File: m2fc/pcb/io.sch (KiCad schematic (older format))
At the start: 28 parts

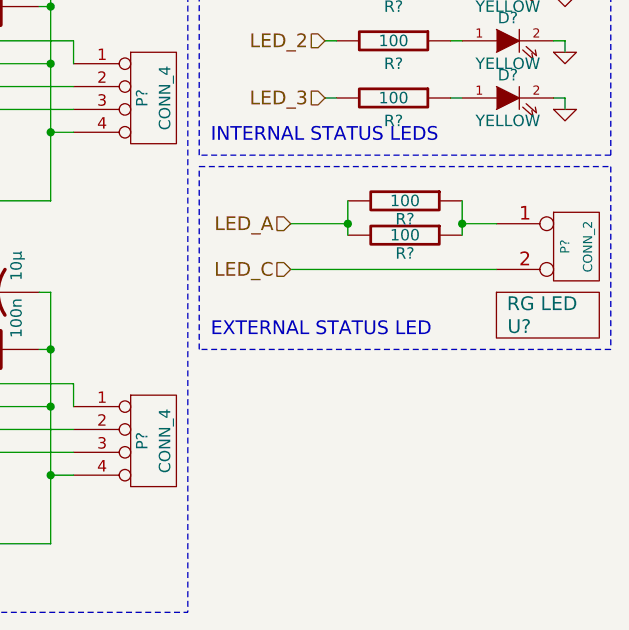
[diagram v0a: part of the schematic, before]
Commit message: rename m2d to m2fc which now incorporates m2p
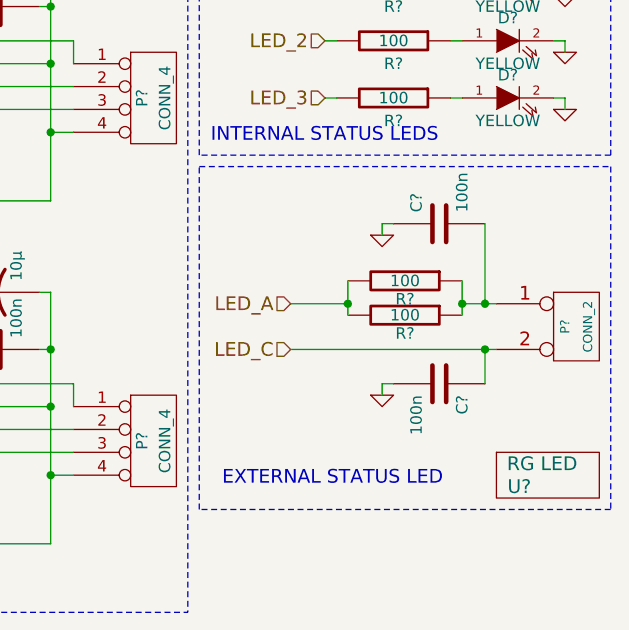
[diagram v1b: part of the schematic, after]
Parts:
- added C? (x2): 100n, 0603, symbol C
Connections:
- net GND: now also C?.1, C?.2
- net LED_C: now also C?.1
- net at P?.1 (P1), R?.1, R?.1: now also C?.2
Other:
- moved on the sheet: P?, R?, U?
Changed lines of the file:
@@
 LIBS:adxl375
 LIBS:apu1205-hf-3
-LIBS:m2d-cache
+LIBS:m2fc-cache
 LIBS:part
 LIBS:sp100-2t
@@
 LIBS:op1177
 LIBS:stm32f415rg
-LIBS:m2d-cache
+LIBS:op2177
+LIBS:microsd
+LIBS:m2fc-cache
 EELAYER 24 0
 EELAYER END
 $Descr A4 11693 8268
 encoding utf-8
-Sheet 5 5
-Title "Martlet 2 Datalogger Board"
-Date "02 Jul 2014"
+Sheet 5 6
+Title "Martlet 2 Flight Computer"
+Date "05 Jul 2014"
 Rev "1"
 Comp "Cambridge University Spaceflight"
@@
 $EndComp
 $Comp
-L GND #PWR?
+L GND #PWR078
 U 1 1 53B6A65A
 P 4200 3400
-F 0 "#PWR?" H 4200 3400 30  0001 C CNN
+F 0 "#PWR078" H 4200 3400 30  0001 C CNN
 F 1 "GND" H 4200 3330 30  0001 C CNN
 F 2 "" H 4200 3400 60  0001 C CNN
@@
 $EndComp
 $Comp
-L GND #PWR?
+L GND #PWR079
 U 1 1 53B6A660
 P 4250 3750
-F 0 "#PWR?" H 4250 3750 30  0001 C CNN
+F 0 "#PWR079" H 4250 3750 30  0001 C CNN
 F 1 "GND" H 4250 3680 30  0001 C CNN
 F 2 "" H 4250 3750 60  0001 C CNN
@@
 $EndComp
 $Comp
-L GND #PWR?
+L GND #PWR080
 U 1 1 53B6A668
 P 3750 3000
-F 0 "#PWR?" H 3750 3000 30  0001 C CNN
+F 0 "#PWR080" H 3750 3000 30  0001 C CNN
 F 1 "GND" H 3750 2930 30  0001 C CNN
 F 2 "" H 3750 3000 60  0001 C CNN
@@
 $EndComp
 $Comp
-L GND #PWR?
+L GND #PWR081
 U 1 1 53B6A69E
 P 4200 4900
-F 0 "#PWR?" H 4200 4900 30  0001 C CNN
+F 0 "#PWR081" H 4200 4900 30  0001 C CNN
 F 1 "GND" H 4200 4830 30  0001 C CNN
 F 2 "" H 4200 4900 60  0001 C CNN
@@
 $EndComp
 $Comp
-L GND #PWR?
+L GND #PWR082
 U 1 1 53B6A6A4
 P 4250 5250
-F 0 "#PWR?" H 4250 5250 30  0001 C CNN
+F 0 "#PWR082" H 4250 5250 30  0001 C CNN
 F 1 "GND" H 4250 5180 30  0001 C CNN
 F 2 "" H 4250 5250 60  0001 C CNN
@@
 $EndComp
 $Comp
-L GND #PWR?
+L GND #PWR083
 U 1 1 53B6A6AC
 P 3750 4500
-F 0 "#PWR?" H 3750 4500 30  0001 C CNN
+F 0 "#PWR083" H 3750 4500 30  0001 C CNN
 F 1 "GND" H 3750 4430 30  0001 C CNN
 F 2 "" H 3750 4500 60  0001 C CNN
@@
 SERIAL IN/OUT
 $Comp
-L +3.3V #PWR?
+L +3.3V #PWR084
 U 1 1 53B6A6B3
 P 4100 5000
-F 0 "#PWR?" H 4100 4960 30  0001 C CNN
+F 0 "#PWR084" H 4100 4960 30  0001 C CNN
 F 1 "+3.3V" H 4100 5110 30  0000 C CNN
 F 2 "" H 4100 5000 60  0000 C CNN
@@
 $EndComp
 $Comp
-L +3.3V #PWR?
+L +3.3V #PWR085
 U 1 1 53B6A6B9
 P 4100 3500
-F 0 "#PWR?" H 4100 3460 30  0001 C CNN
+F 0 "#PWR085" H 4100 3460 30  0001 C CNN
 F 1 "+3.3V" H 4100 3610 30  0000 C CNN
 F 2 "" H 4100 3500 60  0000 C CNN
@@
 Wire Notes Line
 	3300 5500 6300 5500
-Text Notes 6400 4300 0    60   ~ 0
+Text Notes 6450 4950 0    60   ~ 0
 EXTERNAL STATUS LED
 $Comp
 L PART U?
 U 1 1 53B6AD6D
-P 7700 4250
-F 0 "U?" H 7750 4250 60  0000 C CNN
-F 1 "RG LED" H 7850 4350 60  0000 C CNN
-F 2 "" H 7700 4250 60  0001 C CNN
-F 3 "" H 7700 4250 60  0001 C CNN
-F 4 "1142488" H 7700 4250 60  0001 C CNN "Farnell"
-	1    7700 4250
+P 7700 4950
+F 0 "U?" H 7750 4950 60  0000 C CNN
+F 1 "RG LED" H 7850 5050 60  0000 C CNN
+F 2 "" H 7700 4950 60  0001 C CNN
+F 3 "" H 7700 4950 60  0001 C CNN
+F 4 "1142488" H 7700 4950 60  0001 C CNN "Farnell"
+	1    7700 4950
 	1    0    0    -1
 $EndComp
@@
 L CONN_2 P?
 U 1 1 53B6AD75
-P 8000 3900
-F 0 "P?" V 7950 3900 40  0000 C CNN
-F 1 "CONN_2" V 8050 3900 40  0000 C CNN
-F 2 "" H 8000 3900 60  0000 C CNN
-F 3 "" H 8000 3900 60  0000 C CNN
-F 4 "1462926" H 8000 3900 60  0001 C CNN "Farnell"
-	1    8000 3900
+P 8000 4250
+F 0 "P?" V 7950 4250 40  0000 C CNN
+F 1 "CONN_2" V 8050 4250 40  0000 C CNN
+F 2 "" H 8000 4250 60  0000 C CNN
+F 3 "" H 8000 4250 60  0000 C CNN
+F 4 "1462926" H 8000 4250 60  0001 C CNN "Farnell"
+	1    8000 4250
 	1    0    0    -1
 $EndComp
@@
 L R R?
 U 1 1 53B6AD98
-P 7250 3850
-F 0 "R?" V 7330 3850 50  0000 C CNN
-F 1 "100" V 7250 3850 50  0000 C CNN
-F 2 "0603" H 7250 3850 60  0001 C CNN
-F 3 "" H 7250 3850 60  0001 C CNN
-F 4 "2331989" V 7250 3850 60  0001 C CNN "Farnell"
-	1    7250 3850
+P 7250 4200
+F 0 "R?" V 7330 4200 50  0000 C CNN
+F 1 "100" V 7250 4200 50  0000 C CNN
+F 2 "0603" H 7250 4200 60  0001 C CNN
+F 3 "" H 7250 4200 60  0001 C CNN
+F 4 "2331989" V 7250 4200 60  0001 C CNN "Farnell"
+	1    7250 4200
 	0    1    1    0
 $EndComp
@@
 L R R?
 U 1 1 53B6ADA0
-P 7250 3700
-F 0 "R?" V 7330 3700 50  0000 C CNN
-F 1 "100" V 7250 3700 50  0000 C CNN
-F 2 "0603" H 7250 3700 60  0001 C CNN
-F 3 "" H 7250 3700 60  0001 C CNN
-F 4 "2331989" V 7250 3700 60  0001 C CNN "Farnell"
-	1    7250 3700
+P 7250 4050
+F 0 "R?" V 7330 4050 50  0000 C CNN
+F 1 "100" V 7250 4050 50  0000 C CNN
+F 2 "0603" H 7250 4050 60  0001 C CNN
+F 3 "" H 7250 4050 60  0001 C CNN
+F 4 "2331989" V 7250 4050 60  0001 C CNN "Farnell"
+	1    7250 4050
 	0    1    1    0
 $EndComp
 Wire Wire Line
-	6750 4000 7650 4000
-Wire Wire Line
-	7000 3800 6750 3800
-Wire Wire Line
-	7650 3800 7500 3800
+	6750 4350 7650 4350
+Wire Wire Line
+	7000 4150 6750 4150
+Wire Wire Line
+	7500 4150 7650 4150
 Wire Notes Line
 	6350 3550 8150 3550
 Wire Notes Line
-	8150 3550 8150 4350
-Wire Notes Line
-	8150 4350 6350 4350
-Wire Notes Line
-	6350 4350 6350 3550
-Wire Wire Line
-	7000 3700 7000 3850
-Connection ~ 7000 3800
-Wire Wire Line
-	7500 3700 7500 3850
-Connection ~ 7500 3800
+	8150 3550 8150 5050
+Wire Notes Line
+	8150 5050 6350 5050
+Wire Notes Line
+	6350 5050 6350 3550
+Wire Wire Line
+	7000 4050 7000 4200
+Connection ~ 7000 4150
+Wire Wire Line
+	7500 4050 7500 4200
+Connection ~ 7500 4150
 $Comp
 L LED D?
@@
 $EndComp
 $Comp
-L GND #PWR?
+L GND #PWR086
 U 1 1 53B6B193
 P 7600 2550
-F 0 "#PWR?" H 7600 2550 30  0001 C CNN
+F 0 "#PWR086" H 7600 2550 30  0001 C CNN
 F 1 "GND" H 7600 2480 30  0001 C CNN
 F 2 "" H 7600 2550 60  0001 C CNN
@@
 $EndComp
 $Comp
-L GND #PWR?
+L GND #PWR087
 U 1 1 53B6B1AA
 P 7950 2800
-F 0 "#PWR?" H 7950 2800 30  0001 C CNN
+F 0 "#PWR087" H 7950 2800 30  0001 C CNN
 F 1 "GND" H 7950 2730 30  0001 C CNN
 F 2 "" H 7950 2800 60  0001 C CNN
@@
 $EndComp
 $Comp
-L GND #PWR?
+L GND #PWR088
 U 1 1 53B6B1C1
 P 7950 3050
-F 0 "#PWR?" H 7950 3050 30  0001 C CNN
+F 0 "#PWR088" H 7950 3050 30  0001 C CNN
 F 1 "GND" H 7950 2980 30  0001 C CNN
 F 2 "" H 7950 3050 60  0001 C CNN
@@
 $EndComp
 $Comp
-L GND #PWR?
+L GND #PWR089
 U 1 1 53B6B1D8
 P 7950 3300
-F 0 "#PWR?" H 7950 3300 30  0001 C CNN
+F 0 "#PWR089" H 7950 3300 30  0001 C CNN
 F 1 "GND" H 7950 3230 30  0001 C CNN
 F 2 "" H 7950 3300 60  0001 C CNN
@@
 INTERNAL STATUS LEDS
 $Comp
-L +3.3V #PWR?
+L +3.3V #PWR090
 U 1 1 53B6B1DF
 P 6550 2450
-F 0 "#PWR?" H 6550 2410 30  0001 C CNN
+F 0 "#PWR090" H 6550 2410 30  0001 C CNN
 F 1 "+3.3V" H 6550 2560 30  0000 C CNN
 F 2 "" H 6550 2450 60  0000 C CNN
@@
 Text HLabel 3950 4800 0    60   Output ~ 0
 SER_IN_2
-Text HLabel 6750 3800 0    60   Input ~ 0
+Text HLabel 6750 4150 0    60   Input ~ 0
 LED_A
-Text HLabel 6750 4000 0    60   Input ~ 0
+Text HLabel 6750 4350 0    60   Input ~ 0
 LED_C
 Text HLabel 6900 2750 0    60   Input ~ 0
@@
 Connection ~ 4000 3200
 Connection ~ 4000 3300
+$Comp
+L C C?
+U 1 1 53BB2BD1
+P 7400 4500
+F 0 "C?" H 7450 4600 50  0000 L CNN
+F 1 "100n" H 7450 4400 50  0000 L CNN
+F 2 "0603" H 7400 4500 60  0001 C CNN
+F 3 "" H 7400 4500 60  0001 C CNN
+F 4 "1759037" H 7400 4500 60  0001 C CNN "Farnell"
+	1    7400 4500
+	0    1    1    0
+$EndComp
+$Comp
+L C C?
+U 1 1 53BB30F0
+P 7400 3800
+F 0 "C?" H 7450 3900 50  0000 L CNN
+F 1 "100n" H 7450 3700 50  0000 L CNN
+F 2 "0603" H 7400 3800 60  0001 C CNN
+F 3 "" H 7400 3800 60  0001 C CNN
+F 4 "1759037" H 7400 3800 60  0001 C CNN "Farnell"
+	1    7400 3800
+	0    -1   -1   0
+$EndComp
+Wire Wire Line
+	7600 4350 7600 4500
+Connection ~ 7600 4350
+$Comp
+L GND #PWR?
+U 1 1 53BB3222
+P 7150 4550
+F 0 "#PWR?" H 7150 4550 30  0001 C CNN
+F 1 "GND" H 7150 4480 30  0001 C CNN
+F 2 "" H 7150 4550 60  0001 C CNN
+F 3 "" H 7150 4550 60  0001 C CNN
+	1    7150 4550
+	1    0    0    -1
+$EndComp
+Wire Wire Line
+	7200 4500 7150 4500
+Wire Wire Line
+	7150 4500 7150 4550
+$Comp
+L GND #PWR?
+U 1 1 53BB32F5
+P 7150 3850
+F 0 "#PWR?" H 7150 3850 30  0001 C CNN
+F 1 "GND" H 7150 3780 30  0001 C CNN
+F 2 "" H 7150 3850 60  0001 C CNN
+F 3 "" H 7150 3850 60  0001 C CNN
+	1    7150 3850
+	1    0    0    -1
+$EndComp
+Wire Wire Line
+	7600 3800 7600 4150
+Connection ~ 7600 4150
+Wire Wire Line
+	7200 3800 7150 3800
+Wire Wire Line
+	7150 3800 7150 3850
 $EndSCHEMATC

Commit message: update more bits on flight computer..
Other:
- note added: "INPUT/OUTPUT"
- moved on the sheet: C?, P?, R?, U?
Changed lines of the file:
@@
 LIBS:op2177
 LIBS:microsd
+LIBS:adp3335
+LIBS:ad8541
+LIBS:ad8656
+LIBS:stm32f405vgt
 LIBS:m2fc-cache
 EELAYER 24 0
@@
 Wire Notes Line
 	3300 5500 6300 5500
-Text Notes 6450 4950 0    60   ~ 0
+Text Notes 6400 5450 0    60   ~ 0
 EXTERNAL STATUS LED
 $Comp
 L PART U?
 U 1 1 53B6AD6D
-P 7700 4950
-F 0 "U?" H 7750 4950 60  0000 C CNN
-F 1 "RG LED" H 7850 5050 60  0000 C CNN
-F 2 "" H 7700 4950 60  0001 C CNN
-F 3 "" H 7700 4950 60  0001 C CNN
-F 4 "1142488" H 7700 4950 60  0001 C CNN "Farnell"
-	1    7700 4950
+P 7700 4850
+F 0 "U?" H 7750 4850 60  0000 C CNN
+F 1 "RG LED" H 7850 4950 60  0000 C CNN
+F 2 "" H 7700 4850 60  0001 C CNN
+F 3 "" H 7700 4850 60  0001 C CNN
+F 4 "1142488" H 7700 4850 60  0001 C CNN "Farnell"
+	1    7700 4850
 	1    0    0    -1
 $EndComp
@@
 L CONN_2 P?
 U 1 1 53B6AD75
-P 8000 4250
-F 0 "P?" V 7950 4250 40  0000 C CNN
-F 1 "CONN_2" V 8050 4250 40  0000 C CNN
-F 2 "" H 8000 4250 60  0000 C CNN
-F 3 "" H 8000 4250 60  0000 C CNN
-F 4 "1462926" H 8000 4250 60  0001 C CNN "Farnell"
-	1    8000 4250
+P 8000 4500
+F 0 "P?" V 7950 4500 40  0000 C CNN
+F 1 "CONN_2" V 8050 4500 40  0000 C CNN
+F 2 "" H 8000 4500 60  0000 C CNN
+F 3 "" H 8000 4500 60  0000 C CNN
+F 4 "1462926" H 8000 4500 60  0001 C CNN "Farnell"
+	1    8000 4500
 	1    0    0    -1
 $EndComp
@@
 L R R?
 U 1 1 53B6AD98
-P 7250 4200
-F 0 "R?" V 7330 4200 50  0000 C CNN
-F 1 "100" V 7250 4200 50  0000 C CNN
-F 2 "0603" H 7250 4200 60  0001 C CNN
-F 3 "" H 7250 4200 60  0001 C CNN
-F 4 "2331989" V 7250 4200 60  0001 C CNN "Farnell"
-	1    7250 4200
+P 7250 4450
+F 0 "R?" V 7330 4450 50  0000 C CNN
+F 1 "100" V 7250 4450 50  0000 C CNN
+F 2 "0603" H 7250 4450 60  0001 C CNN
+F 3 "" H 7250 4450 60  0001 C CNN
+F 4 "2331989" V 7250 4450 60  0001 C CNN "Farnell"
+	1    7250 4450
 	0    1    1    0
 $EndComp
@@
 L R R?
 U 1 1 53B6ADA0
-P 7250 4050
-F 0 "R?" V 7330 4050 50  0000 C CNN
-F 1 "100" V 7250 4050 50  0000 C CNN
-F 2 "0603" H 7250 4050 60  0001 C CNN
-F 3 "" H 7250 4050 60  0001 C CNN
-F 4 "2331989" V 7250 4050 60  0001 C CNN "Farnell"
-	1    7250 4050
+P 7250 4300
+F 0 "R?" V 7330 4300 50  0000 C CNN
+F 1 "100" V 7250 4300 50  0000 C CNN
+F 2 "0603" H 7250 4300 60  0001 C CNN
+F 3 "" H 7250 4300 60  0001 C CNN
+F 4 "2331989" V 7250 4300 60  0001 C CNN "Farnell"
+	1    7250 4300
 	0    1    1    0
 $EndComp
 Wire Wire Line
-	6750 4350 7650 4350
-Wire Wire Line
-	7000 4150 6750 4150
-Wire Wire Line
-	7500 4150 7650 4150
+	6750 4600 7650 4600
+Wire Wire Line
+	7000 4400 6750 4400
+Wire Wire Line
+	7500 4400 7650 4400
 Wire Notes Line
 	6350 3550 8150 3550
 Wire Notes Line
-	8150 3550 8150 5050
-Wire Notes Line
-	8150 5050 6350 5050
-Wire Notes Line
-	6350 5050 6350 3550
-Wire Wire Line
-	7000 4050 7000 4200
-Connection ~ 7000 4150
-Wire Wire Line
-	7500 4050 7500 4200
-Connection ~ 7500 4150
+	8150 3550 8150 5500
+Wire Notes Line
+	8150 5500 6350 5500
+Wire Notes Line
+	6350 5500 6350 3550
+Wire Wire Line
+	7000 4300 7000 4450
+Connection ~ 7000 4400
+Wire Wire Line
+	7500 4300 7500 4450
+Connection ~ 7500 4400
 $Comp
 L LED D?
@@
 Text HLabel 3950 4800 0    60   Output ~ 0
 SER_IN_2
-Text HLabel 6750 4150 0    60   Input ~ 0
+Text HLabel 6750 4400 0    60   Input ~ 0
 LED_A
-Text HLabel 6750 4350 0    60   Input ~ 0
+Text HLabel 6750 4600 0    60   Input ~ 0
 LED_C
 Text HLabel 6900 2750 0    60   Input ~ 0
@@
 L C C?
 U 1 1 53BB2BD1
-P 7400 4500
-F 0 "C?" H 7450 4600 50  0000 L CNN
-F 1 "100n" H 7450 4400 50  0000 L CNN
-F 2 "0603" H 7400 4500 60  0001 C CNN
-F 3 "" H 7400 4500 60  0001 C CNN
-F 4 "1759037" H 7400 4500 60  0001 C CNN "Farnell"
-	1    7400 4500
+P 7400 4750
+F 0 "C?" H 7450 4850 50  0000 L CNN
+F 1 "100n" H 7450 4650 50  0000 L CNN
+F 2 "0603" H 7400 4750 60  0001 C CNN
+F 3 "" H 7400 4750 60  0001 C CNN
+F 4 "1759037" H 7400 4750 60  0001 C CNN "Farnell"
+	1    7400 4750
 	0    1    1    0
 $EndComp
@@
 L C C?
 U 1 1 53BB30F0
-P 7400 3800
-F 0 "C?" H 7450 3900 50  0000 L CNN
-F 1 "100n" H 7450 3700 50  0000 L CNN
-F 2 "0603" H 7400 3800 60  0001 C CNN
-F 3 "" H 7400 3800 60  0001 C CNN
-F 4 "1759037" H 7400 3800 60  0001 C CNN "Farnell"
-	1    7400 3800
-	0    -1   -1   0
-$EndComp
-Wire Wire Line
-	7600 4350 7600 4500
-Connection ~ 7600 4350
+P 7400 4050
+F 0 "C?" H 7450 4150 50  0000 L CNN
+F 1 "100n" H 7450 3950 50  0000 L CNN
+F 2 "0603" H 7400 4050 60  0001 C CNN
+F 3 "" H 7400 4050 60  0001 C CNN
+F 4 "1759037" H 7400 4050 60  0001 C CNN "Farnell"
+	1    7400 4050
+	0    -1   -1   0
+$EndComp
+Wire Wire Line
+	7600 4600 7600 4750
+Connection ~ 7600 4600
 $Comp
 L GND #PWR?
 U 1 1 53BB3222
-P 7150 4550
-F 0 "#PWR?" H 7150 4550 30  0001 C CNN
-F 1 "GND" H 7150 4480 30  0001 C CNN
-F 2 "" H 7150 4550 60  0001 C CNN
-F 3 "" H 7150 4550 60  0001 C CNN
-	1    7150 4550
-	1    0    0    -1
-$EndComp
-Wire Wire Line
-	7200 4500 7150 4500
-Wire Wire Line
-	7150 4500 7150 4550
+P 7150 4800
+F 0 "#PWR?" H 7150 4800 30  0001 C CNN
+F 1 "GND" H 7150 4730 30  0001 C CNN
+F 2 "" H 7150 4800 60  0001 C CNN
+F 3 "" H 7150 4800 60  0001 C CNN
+	1    7150 4800
+	1    0    0    -1
+$EndComp
+Wire Wire Line
+	7200 4750 7150 4750
+Wire Wire Line
+	7150 4750 7150 4800
 $Comp
 L GND #PWR?
 U 1 1 53BB32F5
-P 7150 3850
-F 0 "#PWR?" H 7150 3850 30  0001 C CNN
-F 1 "GND" H 7150 3780 30  0001 C CNN
-F 2 "" H 7150 3850 60  0001 C CNN
-F 3 "" H 7150 3850 60  0001 C CNN
-	1    7150 3850
-	1    0    0    -1
-$EndComp
-Wire Wire Line
-	7600 3800 7600 4150
-Connection ~ 7600 4150
-Wire Wire Line
-	7200 3800 7150 3800
-Wire Wire Line
-	7150 3800 7150 3850
+P 7150 4100
+F 0 "#PWR?" H 7150 4100 30  0001 C CNN
+F 1 "GND" H 7150 4030 30  0001 C CNN
+F 2 "" H 7150 4100 60  0001 C CNN
+F 3 "" H 7150 4100 60  0001 C CNN
+	1    7150 4100
+	1    0    0    -1
+$EndComp
+Wire Wire Line
+	7600 4050 7600 4400
+Connection ~ 7600 4400
+Wire Wire Line
+	7200 4050 7150 4050
+Wire Wire Line
+	7150 4050 7150 4100
+Text Notes 3350 2250 0    100  ~ 0
+INPUT/OUTPUT
 $EndSCHEMATC

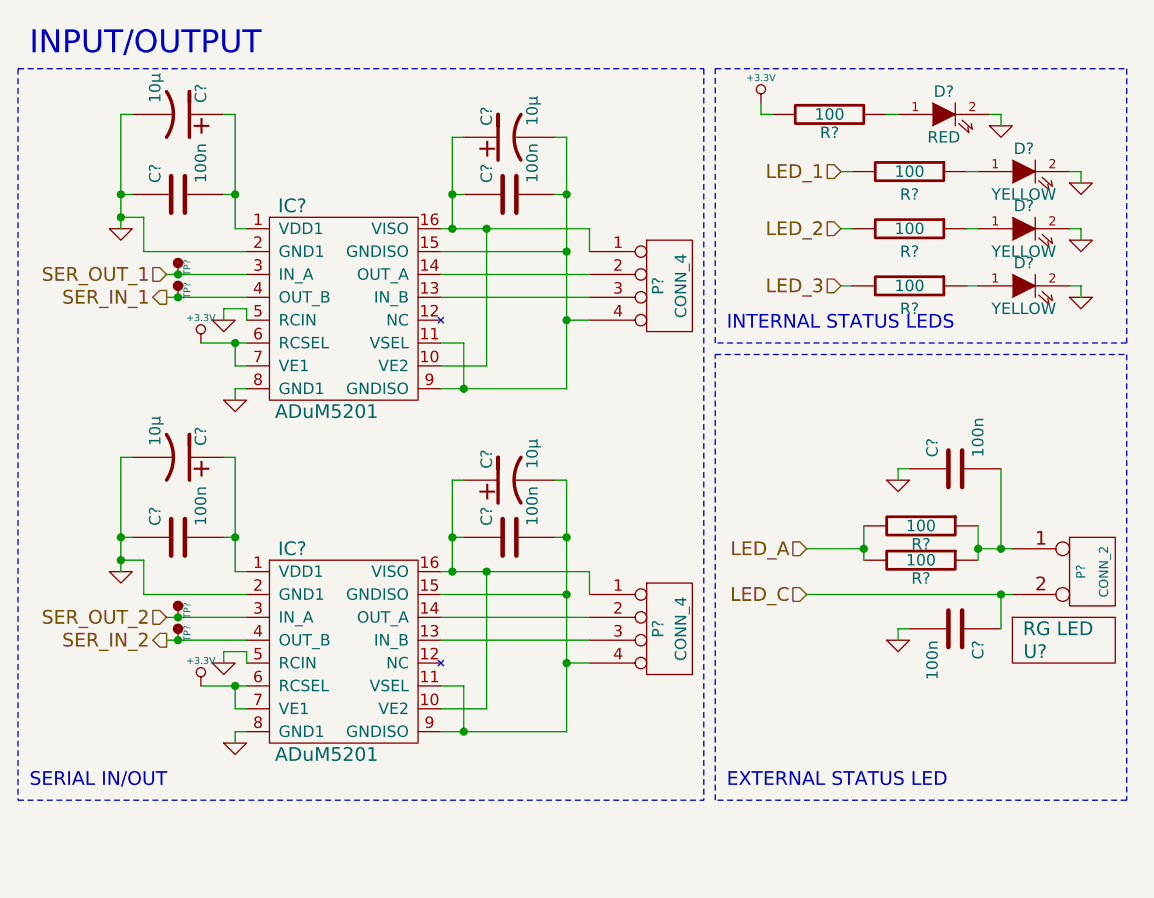
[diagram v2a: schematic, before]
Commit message: fix all the erc errors
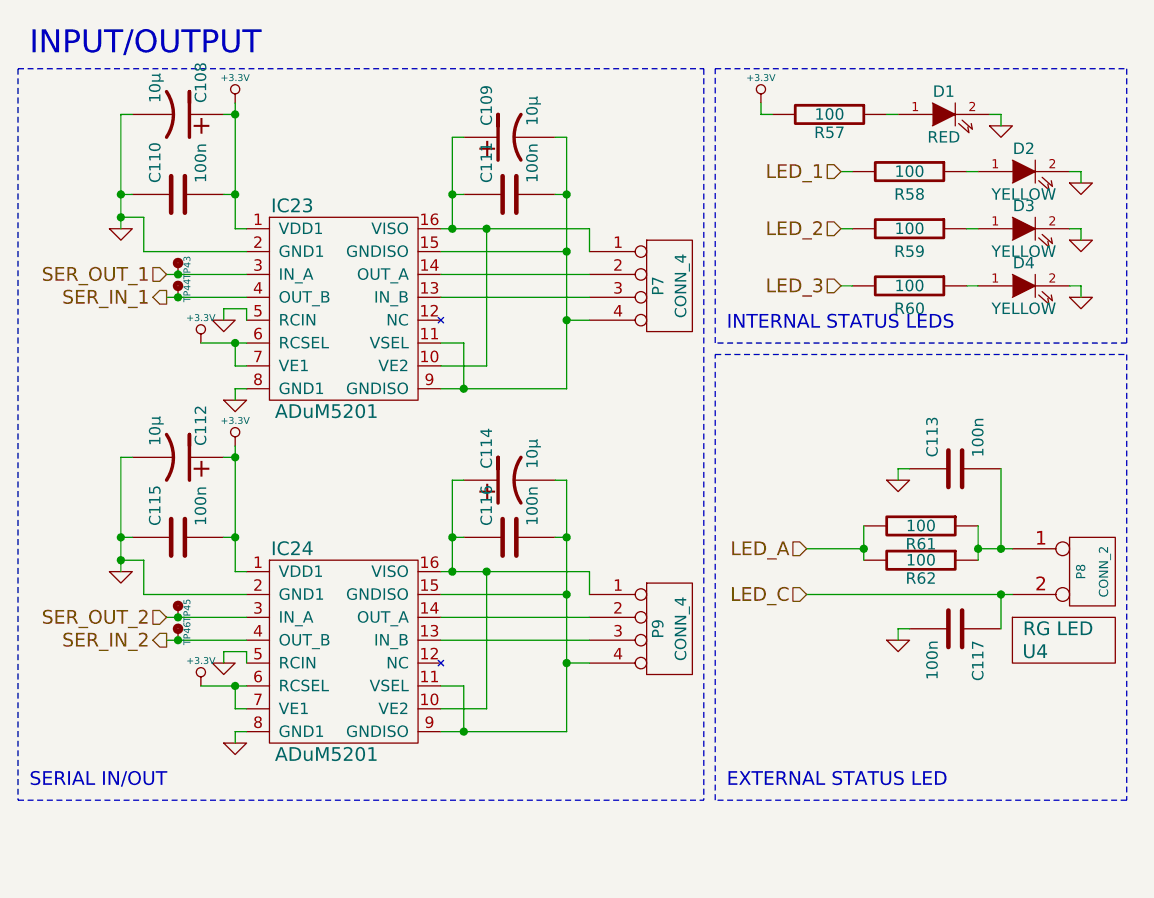
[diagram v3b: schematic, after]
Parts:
- gave numbers to parts that had none: 30
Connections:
- net +3.3V: now also C108.1, C110.2, C112.1, C115.2, IC23.1 (VDD1), IC24.1 (VDD1)
